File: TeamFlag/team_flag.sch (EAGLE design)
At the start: 18 parts, among them Q1 IRFML8244, Q2 IRFML8244

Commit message: REVIEW CHECK: Fix name on APM
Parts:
- renumbered U$3 to APM
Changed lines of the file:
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@@
 <part name="LED4" library="pie" deviceset="LED" device="0805" value="RED"/>
 <part name="SUPPLY5" library="pie" deviceset="GND" device=""/>
-<part name="U$3" library="pie" deviceset="ARDUINO_PRO_MICRO" device=""/>
+<part name="APM" library="pie" deviceset="ARDUINO_PRO_MICRO" device=""/>
 <part name="SUPPLY6" library="pie" deviceset="GND" device=""/>
 </parts>
@@
 </instance>
 <instance part="SUPPLY5" gate="GND" x="78.74" y="7.62"/>
-<instance part="U$3" gate="G$1" x="50.8" y="88.9"/>
+<instance part="APM" gate="G$1" x="50.8" y="88.9"/>
 <instance part="SUPPLY6" gate="GND" x="27.94" y="91.44"/>
 </instances>
@@
 </segment>
 <segment>
-<pinref part="U$3" gate="G$1" pin="6"/>
+<pinref part="APM" gate="G$1" pin="6"/>
 <label x="22.86" y="81.28" size="1.778" layer="95"/>
 <wire x1="38.1" y1="81.28" x2="22.86" y2="81.28" width="0.1524" layer="91"/>
@@
 </segment>
 <segment>
-<pinref part="U$3" gate="G$1" pin="GND@0"/>
+<pinref part="APM" gate="G$1" pin="GND@0"/>
 <wire x1="38.1" y1="96.52" x2="27.94" y2="96.52" width="0.1524" layer="91"/>
 <wire x1="27.94" y1="96.52" x2="27.94" y2="93.98" width="0.1524" layer="91"/>
-<pinref part="U$3" gate="G$1" pin="GND@1"/>
+<pinref part="APM" gate="G$1" pin="GND@1"/>
 <wire x1="27.94" y1="93.98" x2="38.1" y2="93.98" width="0.1524" layer="91"/>
 <pinref part="SUPPLY6" gate="GND" pin="GND"/>
@@
 </segment>
 <segment>
-<pinref part="U$3" gate="G$1" pin="GND@2"/>
+<pinref part="APM" gate="G$1" pin="GND@2"/>
 <wire x1="66.04" y1="99.06" x2="81.28" y2="99.06" width="0.1524" layer="91"/>
 <label x="76.2" y="99.06" size="1.778" layer="95"/>
@@
 </segment>
 <segment>
-<pinref part="U$3" gate="G$1" pin="5"/>
+<pinref part="APM" gate="G$1" pin="5"/>
 <label x="22.86" y="83.82" size="1.778" layer="95"/>
 <wire x1="38.1" y1="83.82" x2="22.86" y2="83.82" width="0.1524" layer="91"/>
@@
 </segment>
 <segment>
-<pinref part="U$3" gate="G$1" pin="VCC"/>
+<pinref part="APM" gate="G$1" pin="VCC"/>
 <wire x1="66.04" y1="93.98" x2="81.28" y2="93.98" width="0.1524" layer="91"/>
 <label x="76.2" y="93.98" size="1.778" layer="95"/>
@@
 </segment>
 <segment>
-<pinref part="U$3" gate="G$1" pin="A0"/>
+<pinref part="APM" gate="G$1" pin="A0"/>
 <wire x1="66.04" y1="83.82" x2="81.28" y2="83.82" width="0.1524" layer="91"/>
 <label x="76.2" y="83.82" size="1.778" layer="95"/>
@@
 </segment>
 <segment>
-<pinref part="U$3" gate="G$1" pin="A3"/>
+<pinref part="APM" gate="G$1" pin="A3"/>
 <wire x1="66.04" y1="91.44" x2="81.28" y2="91.44" width="0.1524" layer="91"/>
 <label x="76.2" y="91.44" size="1.778" layer="95"/>
@@
 </segment>
 <segment>
-<pinref part="U$3" gate="G$1" pin="A2"/>
+<pinref part="APM" gate="G$1" pin="A2"/>
 <wire x1="66.04" y1="88.9" x2="81.28" y2="88.9" width="0.1524" layer="91"/>
 <label x="76.2" y="88.9" size="1.778" layer="95"/>
@@
 </segment>
 <segment>
-<pinref part="U$3" gate="G$1" pin="A1"/>
+<pinref part="APM" gate="G$1" pin="A1"/>
 <wire x1="66.04" y1="86.36" x2="81.28" y2="86.36" width="0.1524" layer="91"/>
 <label x="76.2" y="86.36" size="1.778" layer="95"/>

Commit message: Minor fixes everywhere
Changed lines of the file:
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@@
 <part name="Q2" library="pie" deviceset="MOSFET-NCHANNEL" device="SMD" value="IRFML8244"/>
 <part name="SUPPLY1" library="pie" deviceset="GND" device=""/>
-<part name="FRAME1" library="pie" deviceset="FRAME-LETTER" device="">
+<part name="FRAME1" library="pie" deviceset="FRAME_SCHEMATIC" device="">
 <attribute name="AUTHOR" value="Jared P., Aravind K., Sumita G., Casey D."/>
-<attribute name="REVISION" value="9A"/>
+<attribute name="REVISION" value="9B"/>
 </part>
 <part name="R3" library="pie" deviceset="R-US_" device="R0603" value="10k"/>

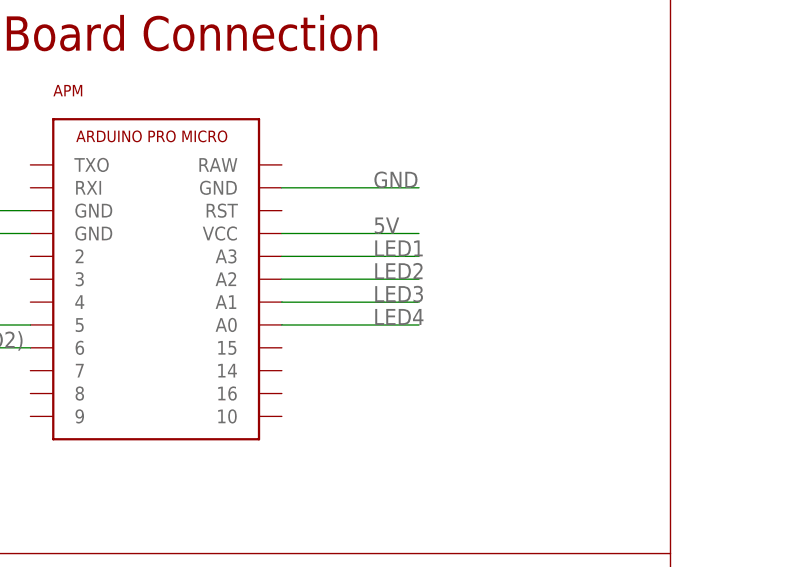
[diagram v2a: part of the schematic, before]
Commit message: APM mirrored and rerouted
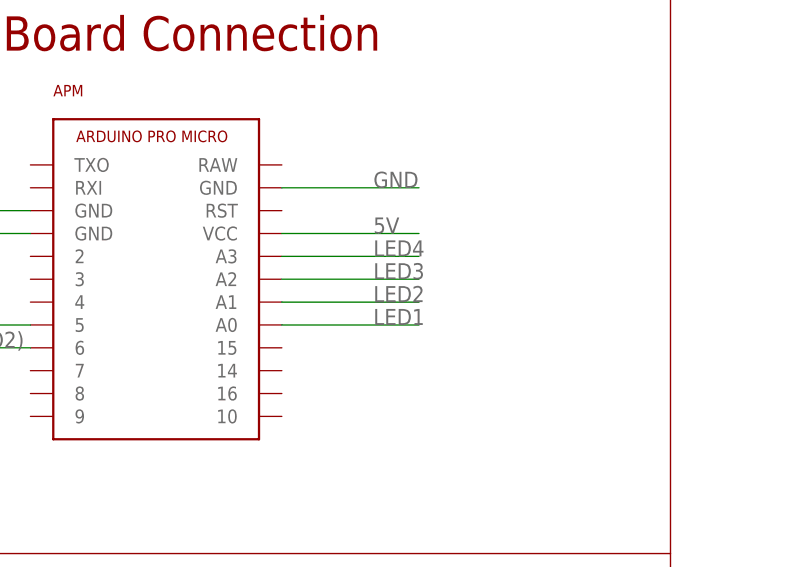
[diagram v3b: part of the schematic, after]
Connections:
- net LED1: now also APM.A0; no longer APM.A3
- net LED2: now also APM.A1; no longer APM.A2
- net LED3: now also APM.A2; no longer APM.A1
- net LED4: now also APM.A3; no longer APM.A0
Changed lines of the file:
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@@
 </segment>
 <segment>
-<pinref part="APM" gate="G$1" pin="A0"/>
-<wire x1="66.04" y1="83.82" x2="81.28" y2="83.82" width="0.1524" layer="91"/>
-<label x="76.2" y="83.82" size="1.778" layer="95"/>
+<pinref part="APM" gate="G$1" pin="A3"/>
+<wire x1="66.04" y1="91.44" x2="81.28" y2="91.44" width="0.1524" layer="91"/>
+<label x="76.2" y="91.44" size="1.778" layer="95"/>
 </segment>
 </net>
@@
 </segment>
 <segment>
-<pinref part="APM" gate="G$1" pin="A3"/>
-<wire x1="66.04" y1="91.44" x2="81.28" y2="91.44" width="0.1524" layer="91"/>
-<label x="76.2" y="91.44" size="1.778" layer="95"/>
+<pinref part="APM" gate="G$1" pin="A0"/>
+<wire x1="66.04" y1="83.82" x2="81.28" y2="83.82" width="0.1524" layer="91"/>
+<label x="76.2" y="83.82" size="1.778" layer="95"/>
 </segment>
 </net>
@@
 </segment>
 <segment>
-<pinref part="APM" gate="G$1" pin="A2"/>
-<wire x1="66.04" y1="88.9" x2="81.28" y2="88.9" width="0.1524" layer="91"/>
-<label x="76.2" y="88.9" size="1.778" layer="95"/>
+<pinref part="APM" gate="G$1" pin="A1"/>
+<wire x1="66.04" y1="86.36" x2="81.28" y2="86.36" width="0.1524" layer="91"/>
+<label x="76.2" y="86.36" size="1.778" layer="95"/>
 </segment>
 </net>
@@
 </segment>
 <segment>
-<pinref part="APM" gate="G$1" pin="A1"/>
-<wire x1="66.04" y1="86.36" x2="81.28" y2="86.36" width="0.1524" layer="91"/>
-<label x="76.2" y="86.36" size="1.778" layer="95"/>
+<pinref part="APM" gate="G$1" pin="A2"/>
+<wire x1="66.04" y1="88.9" x2="81.28" y2="88.9" width="0.1524" layer="91"/>
+<label x="76.2" y="88.9" size="1.778" layer="95"/>
 </segment>
 </net>
